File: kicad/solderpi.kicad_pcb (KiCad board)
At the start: 2 copper layers, 100 x 75 mm, 79 parts, among them J101 CON_ULTRAFIT, J102 Conn_01x07, J103 Conn_01x07, J201 JTAG, J202 OLED, J401 Conn_ARM_JTAG_SWD_10, Q301 NVR4003NT3G, Q302 NVR4003NT3G, Q303 IRF7416TRPBFCT-ND, Q304 IRF7416TRPBFCT-ND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

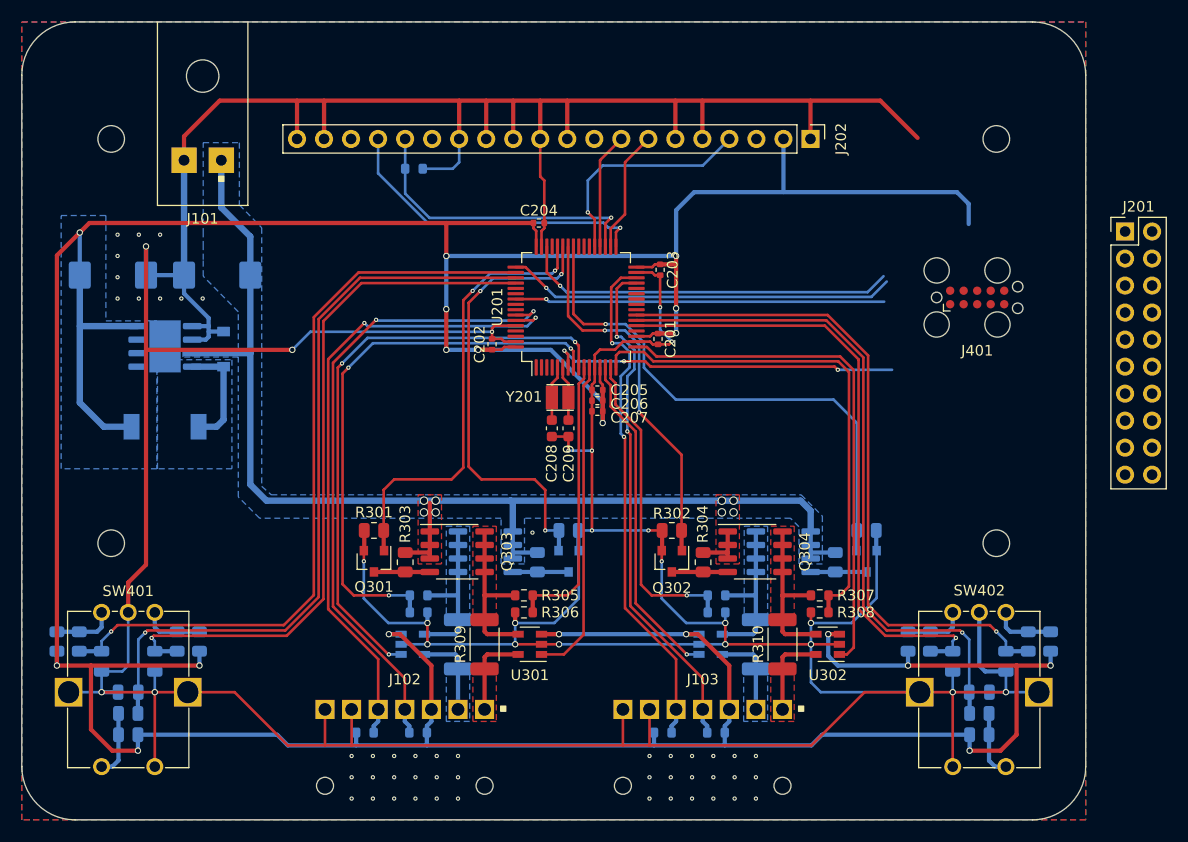
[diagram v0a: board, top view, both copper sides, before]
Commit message: refactored debug connector
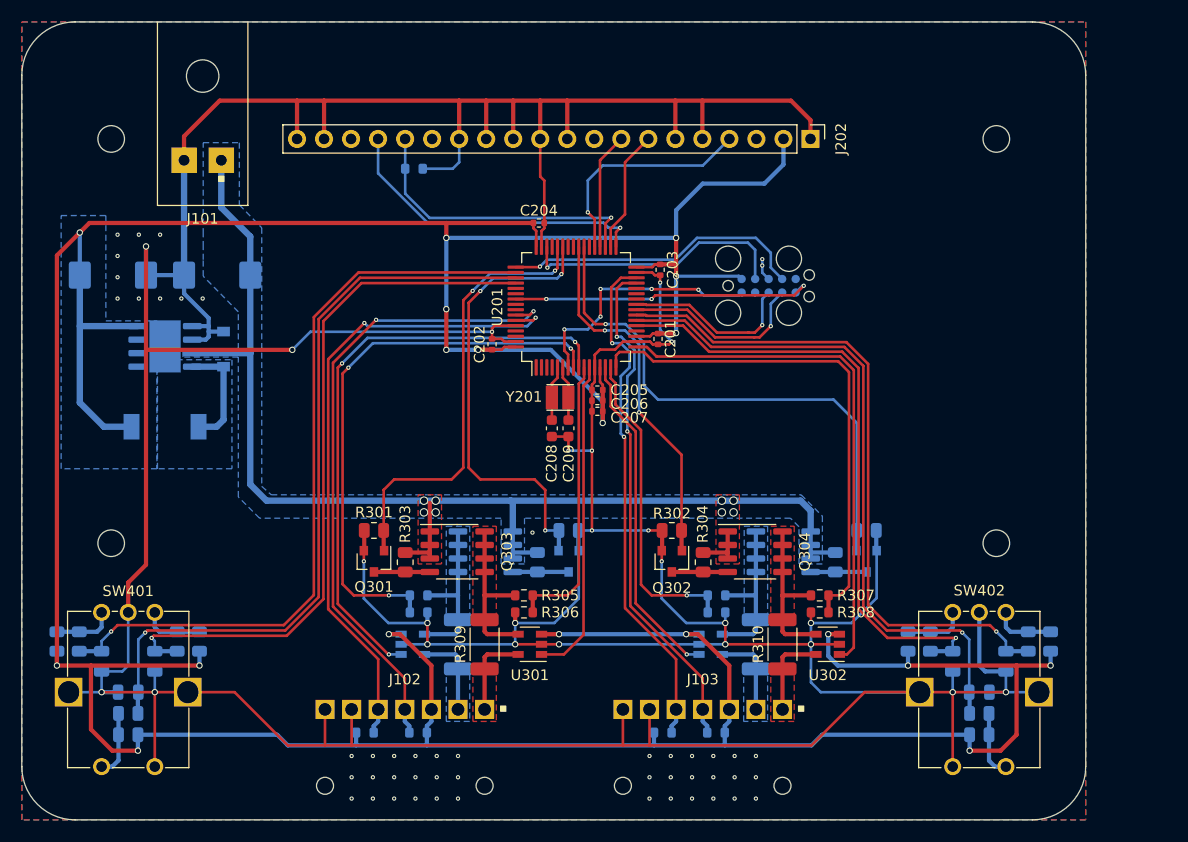
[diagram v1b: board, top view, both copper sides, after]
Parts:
- removed J201: JTAG, Connector_PinHeader_2.54mm:PinHeader_2x10_P2.54mm_Vertical
- J401: moved to B.Cu
- moved J401 19.6 mm to (160.2, 83.8)
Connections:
- J401 pad 1: Net-(J401-Pad1) -> +3V3
- J401 pad 10: Net-(J401-Pad10) -> /mcu/~RESET~
- J401 pad 2: Net-(J401-Pad2) -> /mcu/SWDIO
- J401 pad 3: Net-(J401-Pad3) -> GND
- J401 pad 4: Net-(J401-Pad4) -> /mcu/SWDCLK
- J401 pad 5: Net-(J401-Pad3) -> (no net)
- J401 pad 6: Net-(J401-Pad6) -> /mcu/SWO
- J401 pad 7: Net-(J401-Pad7) -> /mcu/USART_TX
- J401 pad 8: Net-(J401-Pad8) -> /mcu/USART_RX
- U201 pad 24: Net-(U201-Pad24) -> /mcu/USART_TX
- U201 pad 25: Net-(U201-Pad25) -> /mcu/USART_RX
- U201 pad 39: Net-(U201-Pad39) -> /mcu/CHA1_PWM_1
- U201 pad 40: Net-(U201-Pad40) -> /mcu/CHA1_PWM_0
- U201 pad 41: /mcu/CHA1_PWM_1 -> Net-(U201-Pad41)
- U201 pad 42: /mcu/CHA1_PWM_0 -> Net-(U201-Pad42)
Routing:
- net /mcu/USART_TX: track 0.00 -> 17.7 mm, vias 0 -> 1
- net /mcu/USART_RX: track 0.00 -> 16.5 mm, vias 0 -> 1
- net +3V3: track 423.1 -> 408.1 mm
- net GND: track 545.4 -> 534.9 mm, vias 71 -> 73
- net /mcu/SWDIO: track 35.5 -> 25.5 mm
- net /mcu/~RESET~: track 33.3 -> 23.8 mm, vias 3 -> 5
- net /mcu/SWDCLK: track 36.6 -> 28.6 mm
- net /mcu/SWO: track 34.7 -> 28.6 mm, vias 1 -> 3
- net /mcu/CHA1_PWM_0: track 35.4 -> 34.3 mm

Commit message: wip
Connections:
- net /mcu/OLED_~CS~ renamed /mcu/OLED_~{CS}
- net /mcu/OLED_~RESET~ renamed /mcu/OLED_~{RESET}
- net /mcu/~RESET~ renamed /mcu/~{RESET}
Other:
- net class Default removed
- net class mcu removed
